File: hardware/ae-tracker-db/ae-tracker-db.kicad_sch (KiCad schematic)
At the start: 29 parts, among them J1 Conn_01x04_Plug, J2 Conn_01x01_Pin, J3 Conn_01x04_Socket, J4 Conn_01x16_Pin, U1 SN65HVD231, U2 LIS3DH, U3 BQ25176J, U4 TPS1H000-Q1

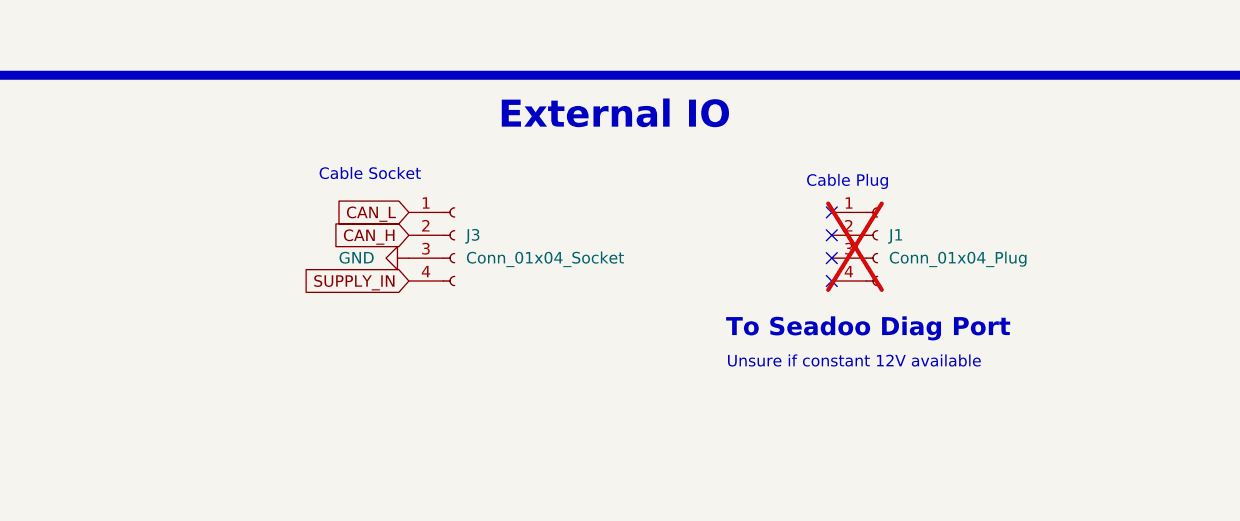
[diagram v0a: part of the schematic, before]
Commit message: feat(hw): update ae-tracker-db schematic, add pinout diagram
Sync ae-tracker-db.kicad_sch/pro/prl for daughter board integration
work, and add a pinout reference image.

Also ignore KiCad's transient lock/autosave files.
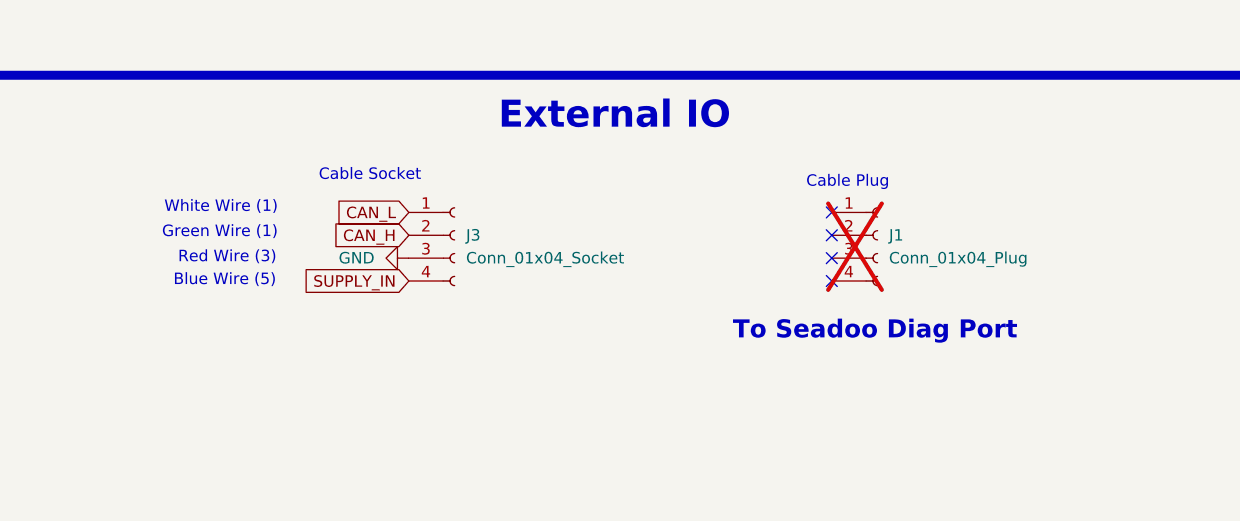
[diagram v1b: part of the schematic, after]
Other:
- note added: "Blue Wire (5)"
- note added: "Green Wire (1)"
- note added: "Red Wire (3)"
- note added: "White Wire (1)"
- note removed: "Unsure if constant 12V available"
